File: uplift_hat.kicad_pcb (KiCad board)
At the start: 2 copper layers, 65 x 30 mm, 4 parts, among them J1 8P8C, J2 8P8C, J3 Raspberry_Pi_2_3

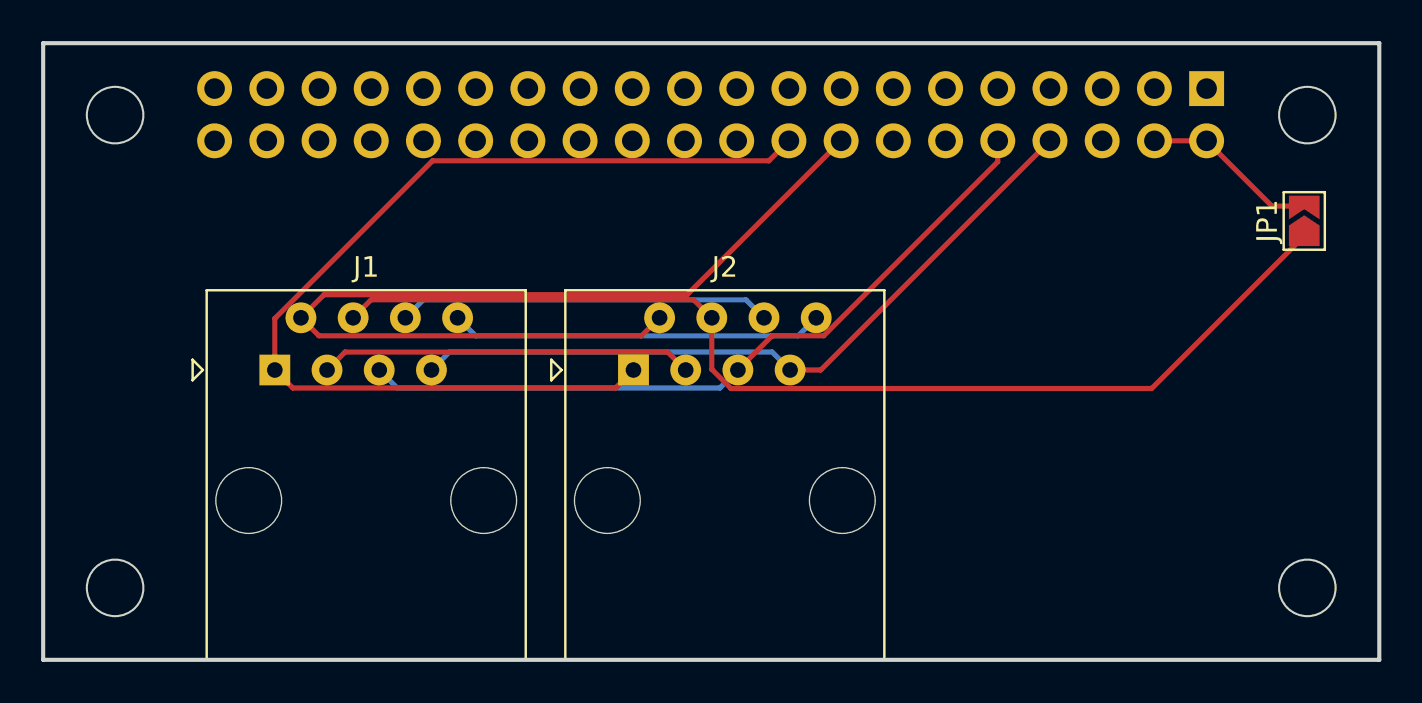
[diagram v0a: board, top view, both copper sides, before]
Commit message: Fixed GPIO orientation
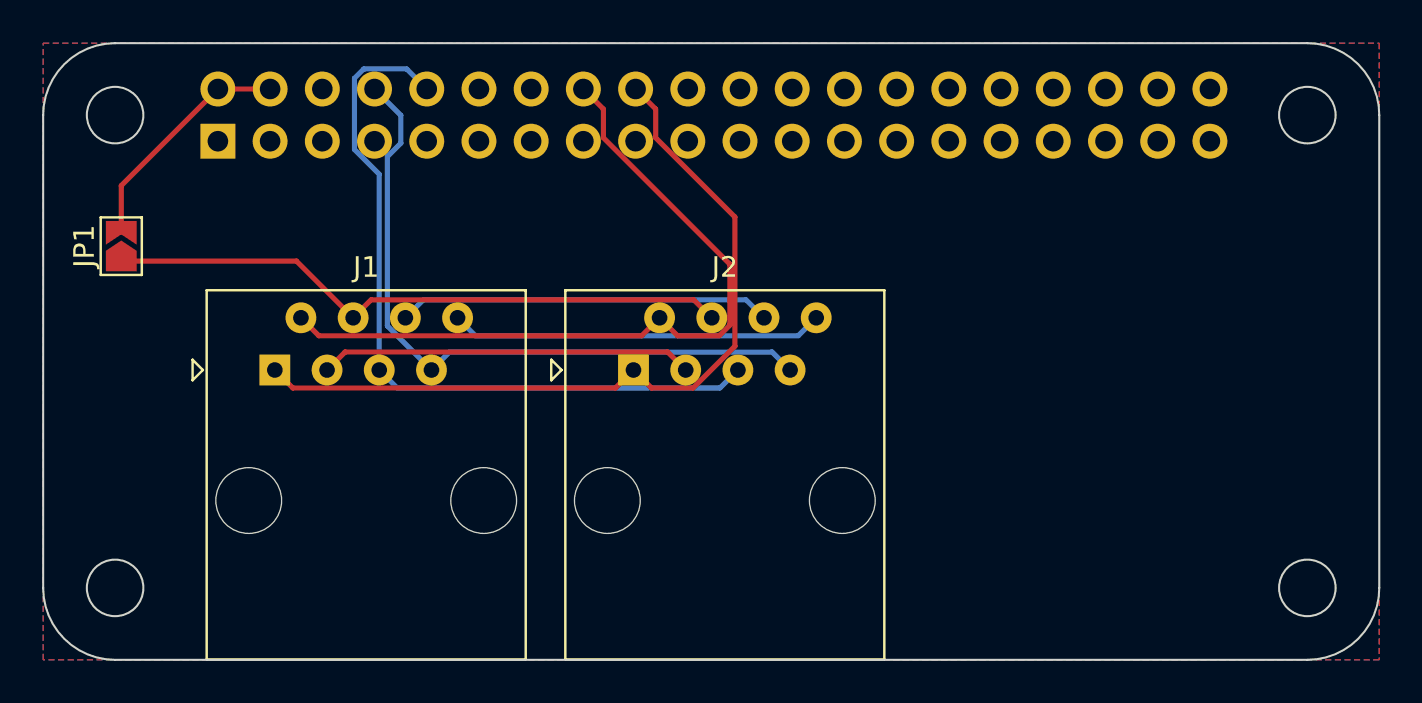
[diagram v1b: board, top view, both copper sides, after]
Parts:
- moved JP1 57.6 mm to (103.8, 109.9)
- moved J3 48.2 mm to (108.5, 104.8), turned to -90 degrees
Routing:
- net +5V: track 53.0 -> 30.6 mm
- net /UP: track 48.0 -> 36.6 mm
- net /DOWN: track 49.3 -> 38.8 mm
- net Net-(J3-Pad2): track 8.61 -> 11.4 mm
- net /UART_RX: track 35.4 -> 33.5 mm
- net /UART_TX: track 36.0 -> 37.0 mm
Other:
- outline, holes or cut-outs redrawn

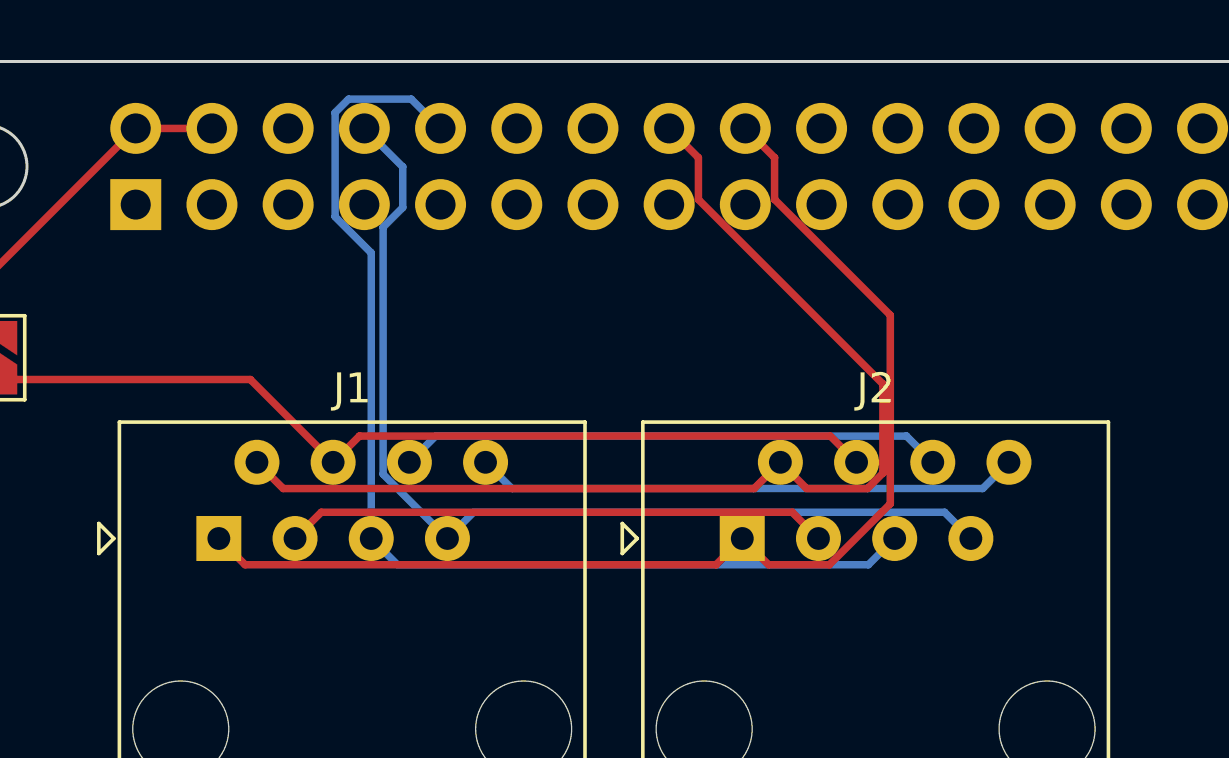
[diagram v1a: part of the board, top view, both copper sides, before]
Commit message: Fixed design rules and generated gerbers
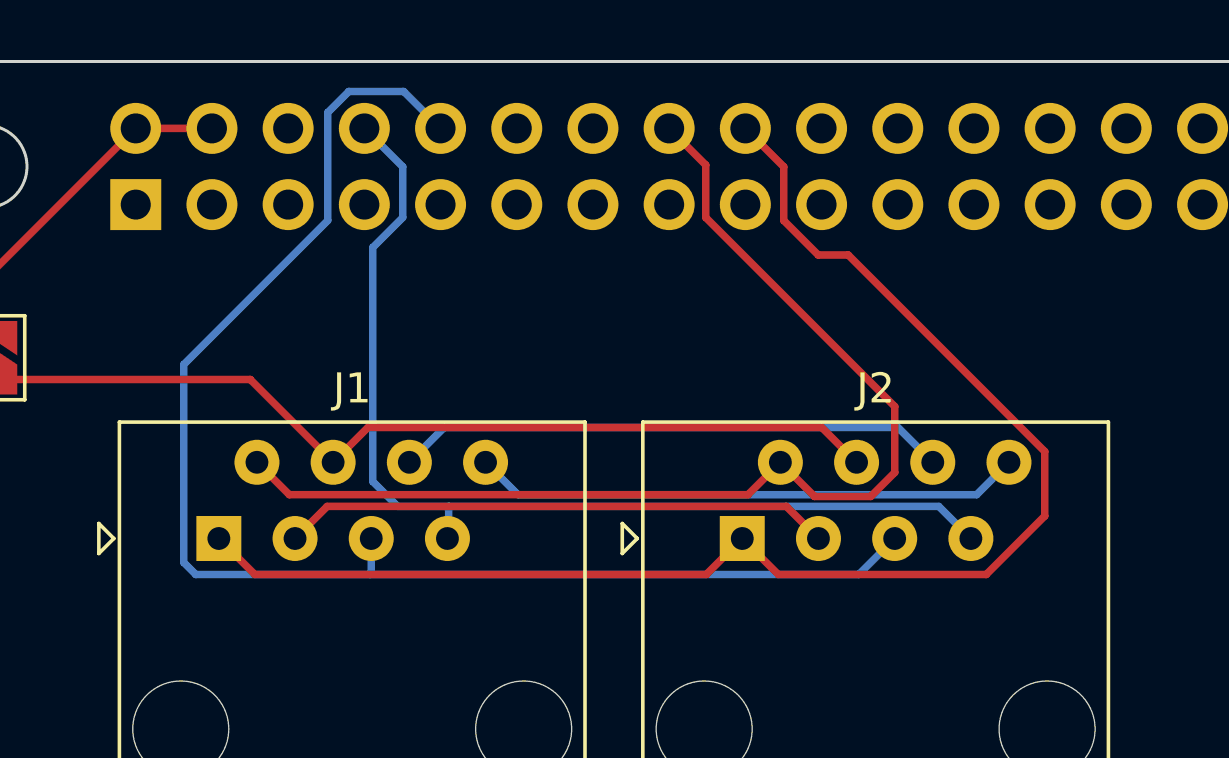
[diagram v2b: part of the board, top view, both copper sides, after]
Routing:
- net /UART_TX: track 37.0 -> 47.1 mm
- net /DOWN: track 38.8 -> 47.5 mm
- net /UART_RX: track 33.5 -> 34.5 mm
- net /UP: track 36.6 -> 37.5 mm
